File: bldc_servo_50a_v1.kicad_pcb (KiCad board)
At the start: 4 copper layers, 100 x 50 mm, 133 parts, among them J1 CAN1, J2 CAN2, J3 FAN, J4 SWD, J5 SWD, P1 PVDD, P2 GND, P3 PHASE_A, P4 PHASE_B, P5 PHASE_C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

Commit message: Placing DRV, Bulk caps, FETs
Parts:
- removed J4: SWD, Connector_PinHeader_2.54mm:PinHeader_1x05_P2.54mm_Vertical
- moved D2 516.9 mm to (-5.00, 93.4)
- moved H1 516.1 mm to (-9.33, 104.2)
- moved H2 516.1 mm to (-9.33, 109.4)
- moved H3 516.1 mm to (-9.33, 114.6)
- moved C47 474.4 mm to (25.4, -53.5)
- moved J3 474.4 mm to (26.1, -65.4)
- moved U6 474.4 mm to (29.4, -55.4)
- moved C53 436.2 mm to (-17.9, 71.5)
- moved R28 436.2 mm to (-18.3, 74.4)
- moved TH1 436.2 mm to (-18.3, 76.4)
- moved C48 435.1 mm to (-39.9, 66.1)
- moved D1 435.1 mm to (-39.9, 62.4)
- moved D3 435.1 mm to (-51.6, 28.4)
- moved D4 435.1 mm to (-51.6, 32.1)
- moved D5 435.1 mm to (-51.6, 35.8)
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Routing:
- net GND: track 56.4 -> 0.35 mm
- net PVDD: track 0.00 -> 1.00 mm

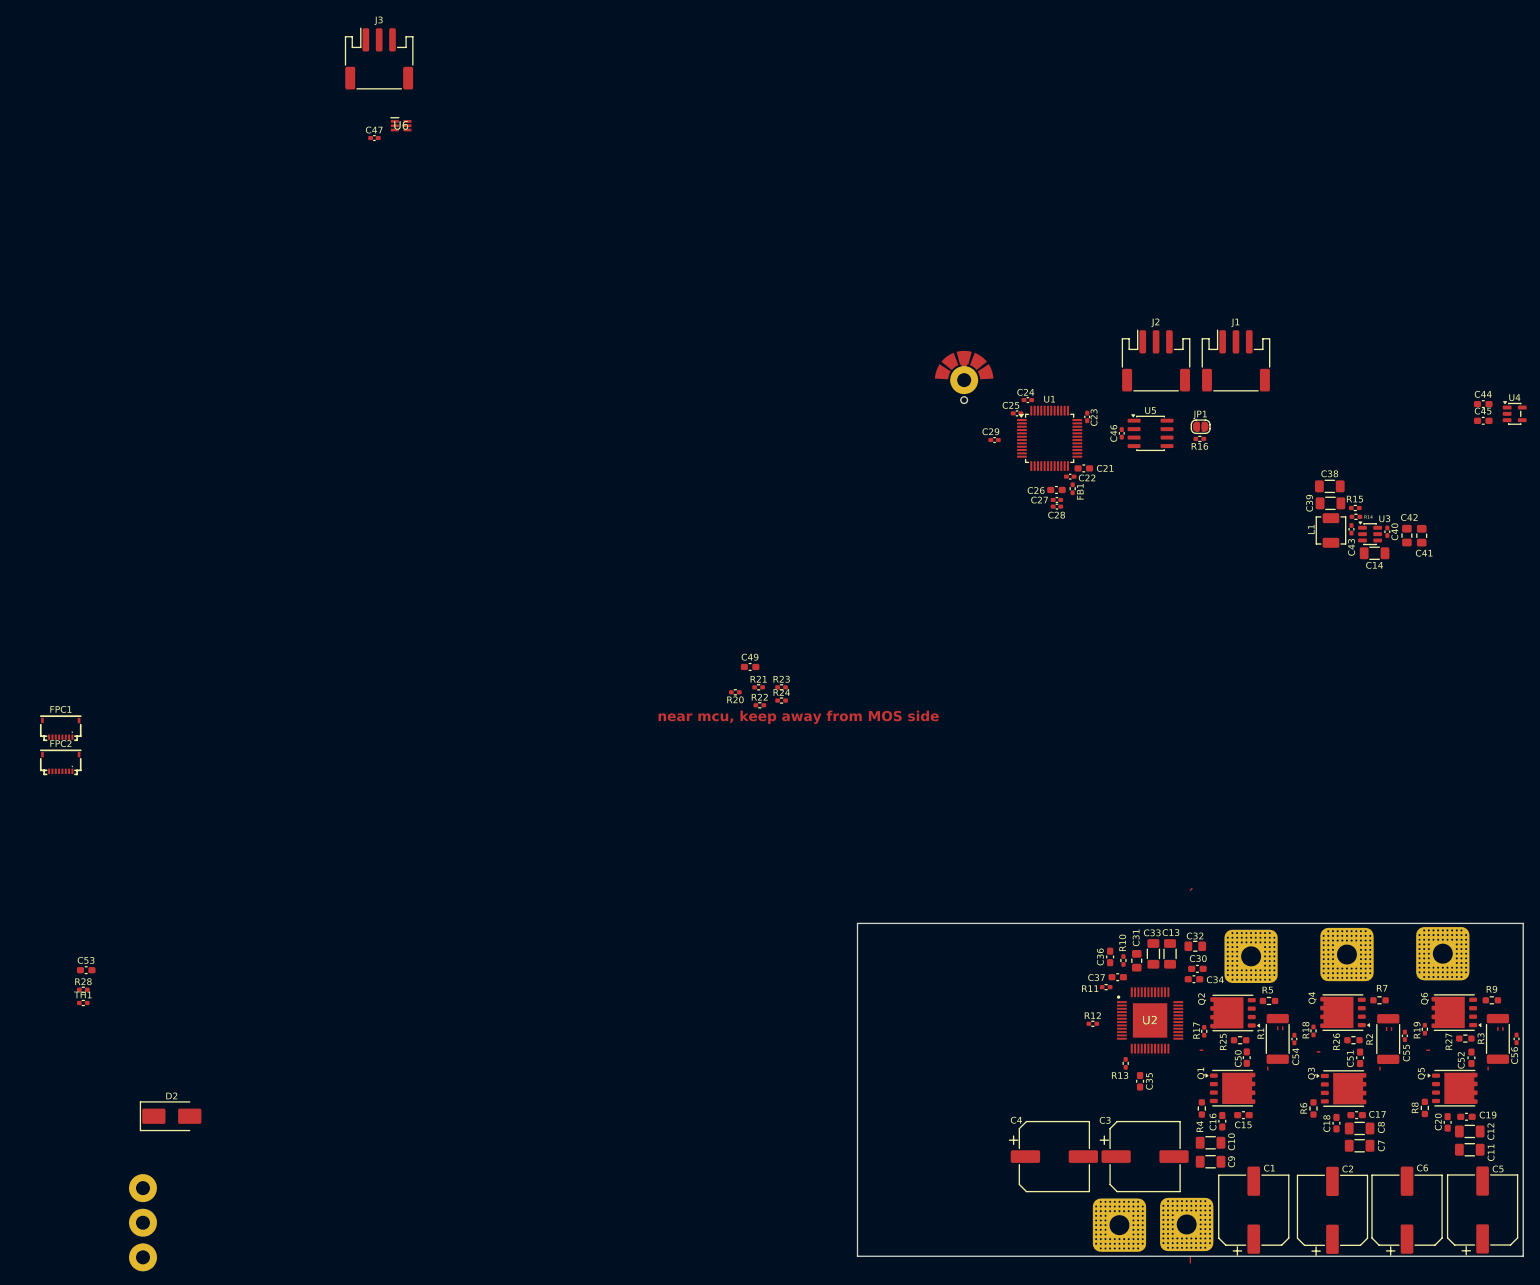
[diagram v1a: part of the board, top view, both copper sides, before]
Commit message: Some more component placement
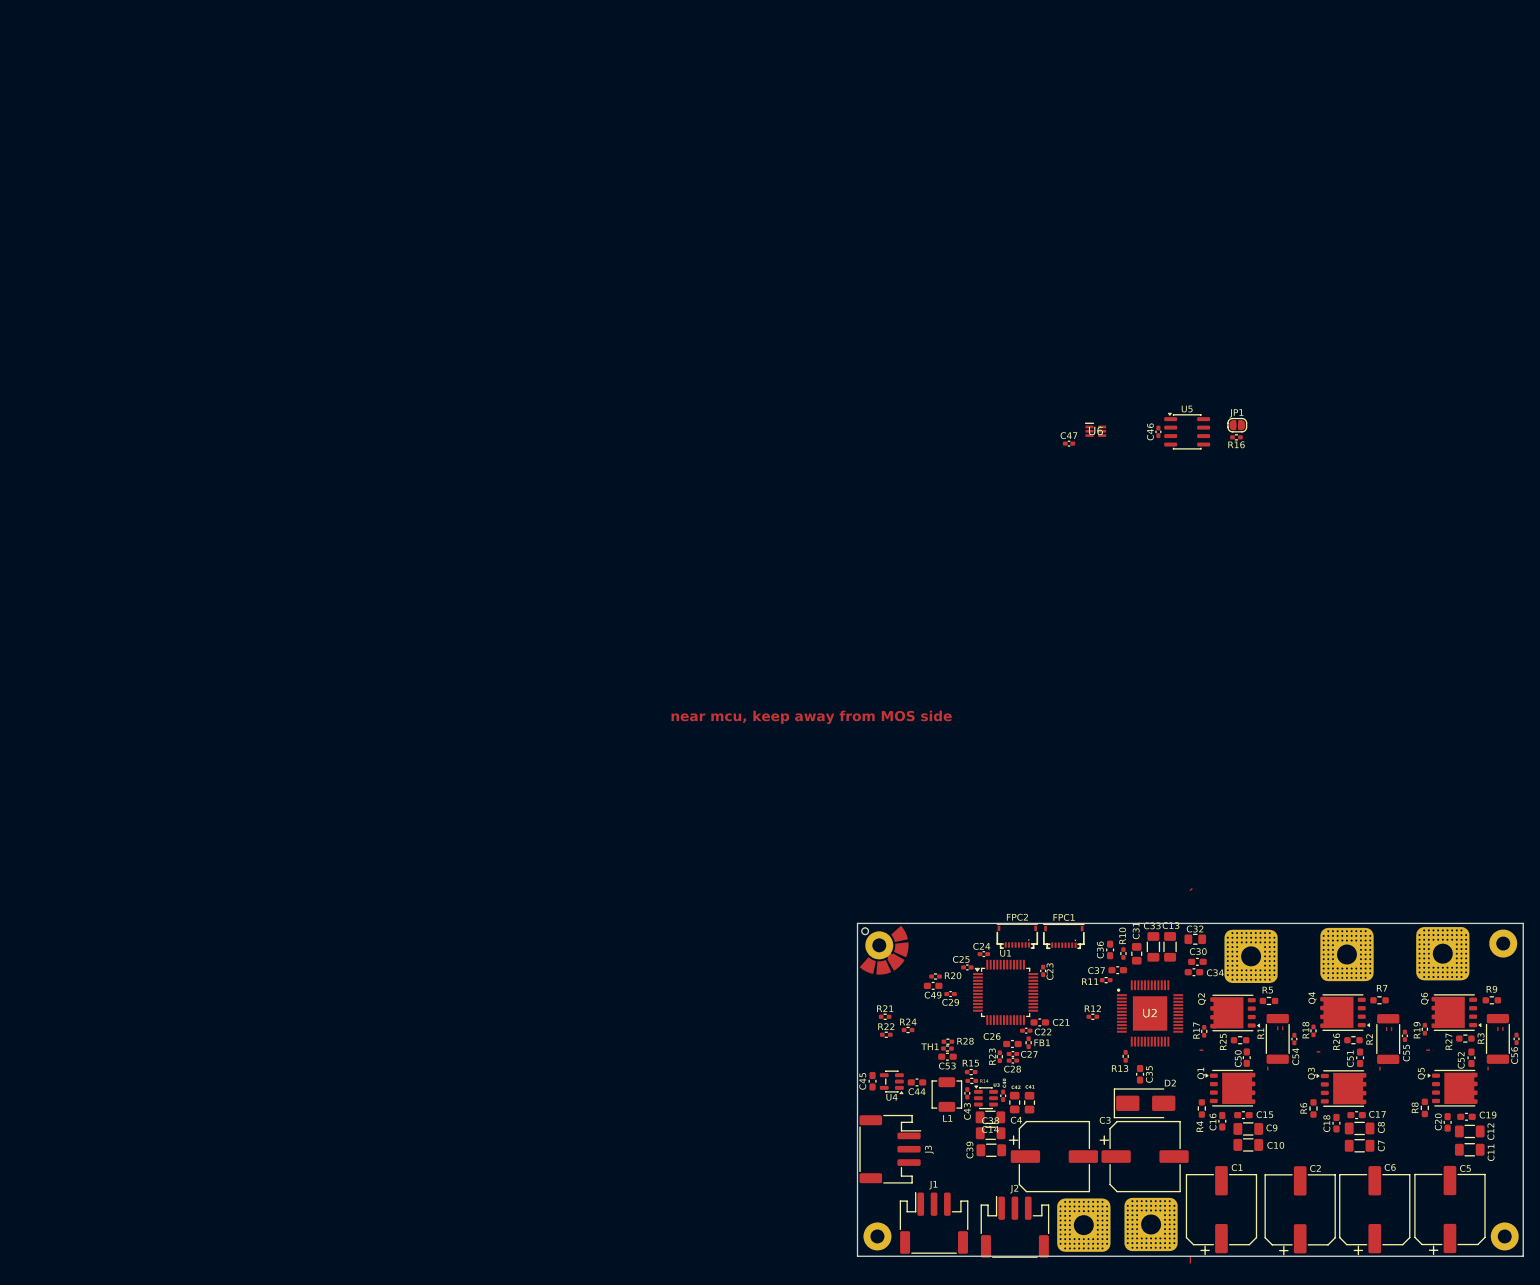
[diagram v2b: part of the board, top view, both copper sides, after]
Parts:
- moved H1 207.6 mm to (195.0, 67.5)
- moved H2 204.6 mm to (195.2, 111.5)
- moved J3 180.9 mm to (102.9, 98.4), turned to -90 degrees
- moved FPC1 153.9 mm to (129.0, 66.5)
- moved D2 146.3 mm to (141.3, 91.5)
- moved FPC2 146.0 mm to (122.0, 66.5)
- moved J1 137.2 mm to (109.5, 109.5)
- moved U4 137.2 mm to (103.2, 88.2), turned to 180 degrees
- moved C45 135.1 mm to (100.3, 88.2), turned to 90 degrees
- moved C44 132.7 mm to (106.9, 88.4), turned to 180 degrees
- moved J2 131.9 mm to (121.7, 110.1)
- moved R28 130.1 mm to (111.6, 82.2)
- moved C53 130.0 mm to (111.5, 84.5), turned to 180 degrees
- moved TH1 130.0 mm to (111.5, 83.3), turned to 180 degrees
- moved U6 114.0 mm to (133.8, -9.45)
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
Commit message: Some routing done
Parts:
- moved H1 125.7 mm to (319.7, 51.2)
- moved P2 125.7 mm to (256.7, 93.5)
- moved C14 125.7 mm to (242.6, 77.3)
- moved C24 125.7 mm to (241.6, 52.8)
- moved C29 125.7 mm to (236.6, 58.8)
- moved C41 125.7 mm to (248.5, 75.1)
- moved C53 125.7 mm to (236.2, 68.2)
- moved FPC2 125.7 mm to (246.7, 50.2)
- moved J5 125.7 mm to (225.9, 51.5)
- moved R22 125.7 mm to (227.0, 64.9)
- moved R23 125.7 mm to (244.0, 68.2)
- moved U4 125.7 mm to (227.8, 72.0)
- moved C21 125.7 mm to (250.0, 63.1)
- moved C22 125.7 mm to (248.0, 64.3)
- moved C23 125.7 mm to (250.6, 55.3)
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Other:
- board size 100 x 50 mm -> 100 x 75 mm

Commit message: Placement of caps
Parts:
- moved C14 176.6 mm to (66.4, 88.5)
- moved C21 176.6 mm to (73.8, 74.2)
- moved C22 176.6 mm to (71.8, 75.5)
- moved C23 176.6 mm to (74.4, 66.5)
- moved C24 176.6 mm to (65.4, 64.0)
- moved C25 176.6 mm to (63.0, 66.0)
- moved C26 176.6 mm to (69.7, 77.5)
- moved C27 176.6 mm to (69.8, 79.0)
- moved C28 176.6 mm to (69.8, 80.0)
- moved C29 176.6 mm to (60.4, 70.0)
- moved C38 176.6 mm to (66.5, 90.9)
- moved C39 176.6 mm to (66.6, 93.4)
- moved C40 176.6 mm to (68.4, 85.3)
- moved C41 176.6 mm to (72.3, 86.3)
- moved C42 176.6 mm to (70.1, 86.3)
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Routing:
- net PVDD: track 1.00 -> 0.00 mm

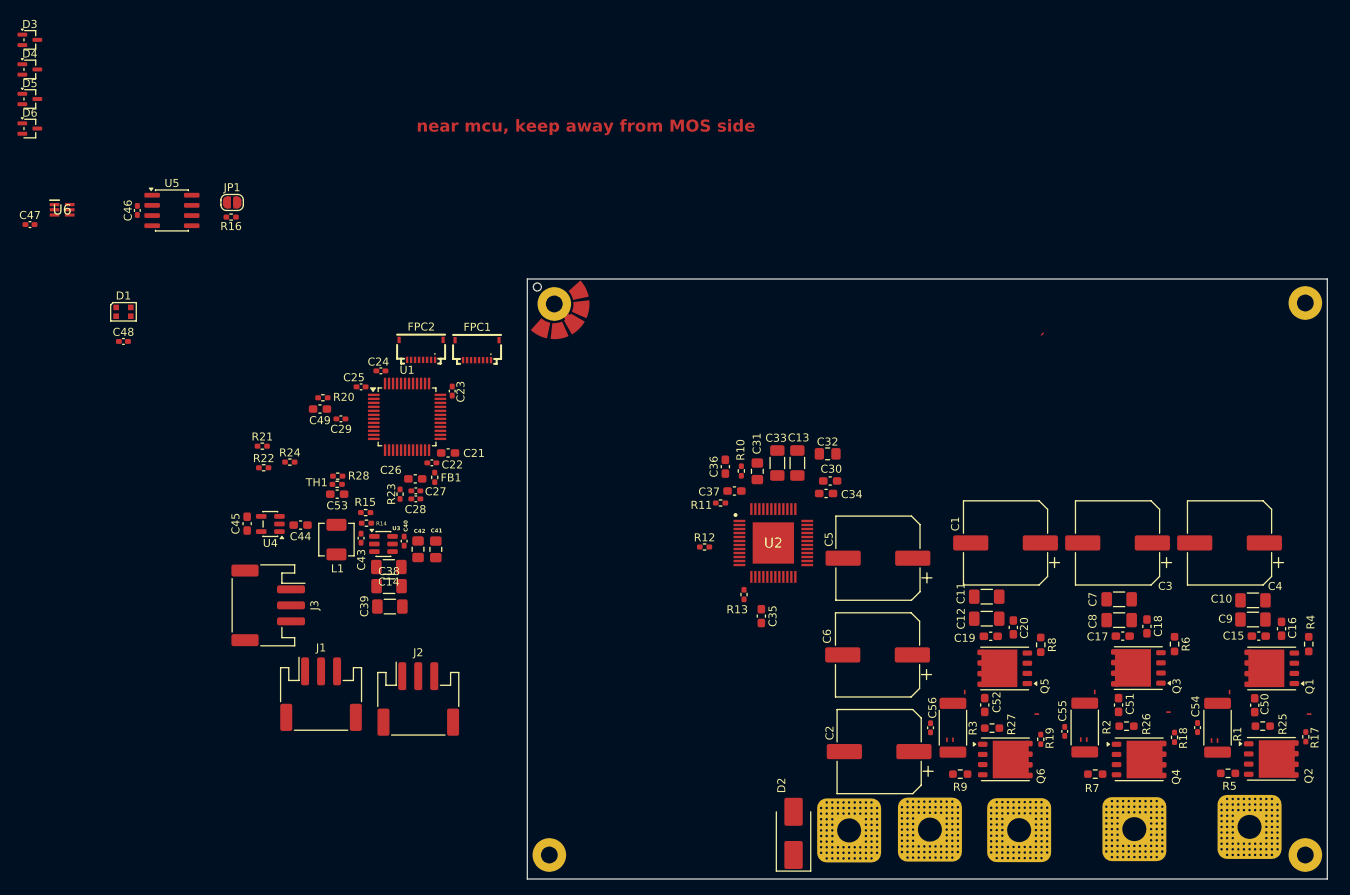
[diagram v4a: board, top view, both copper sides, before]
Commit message: Placement changed
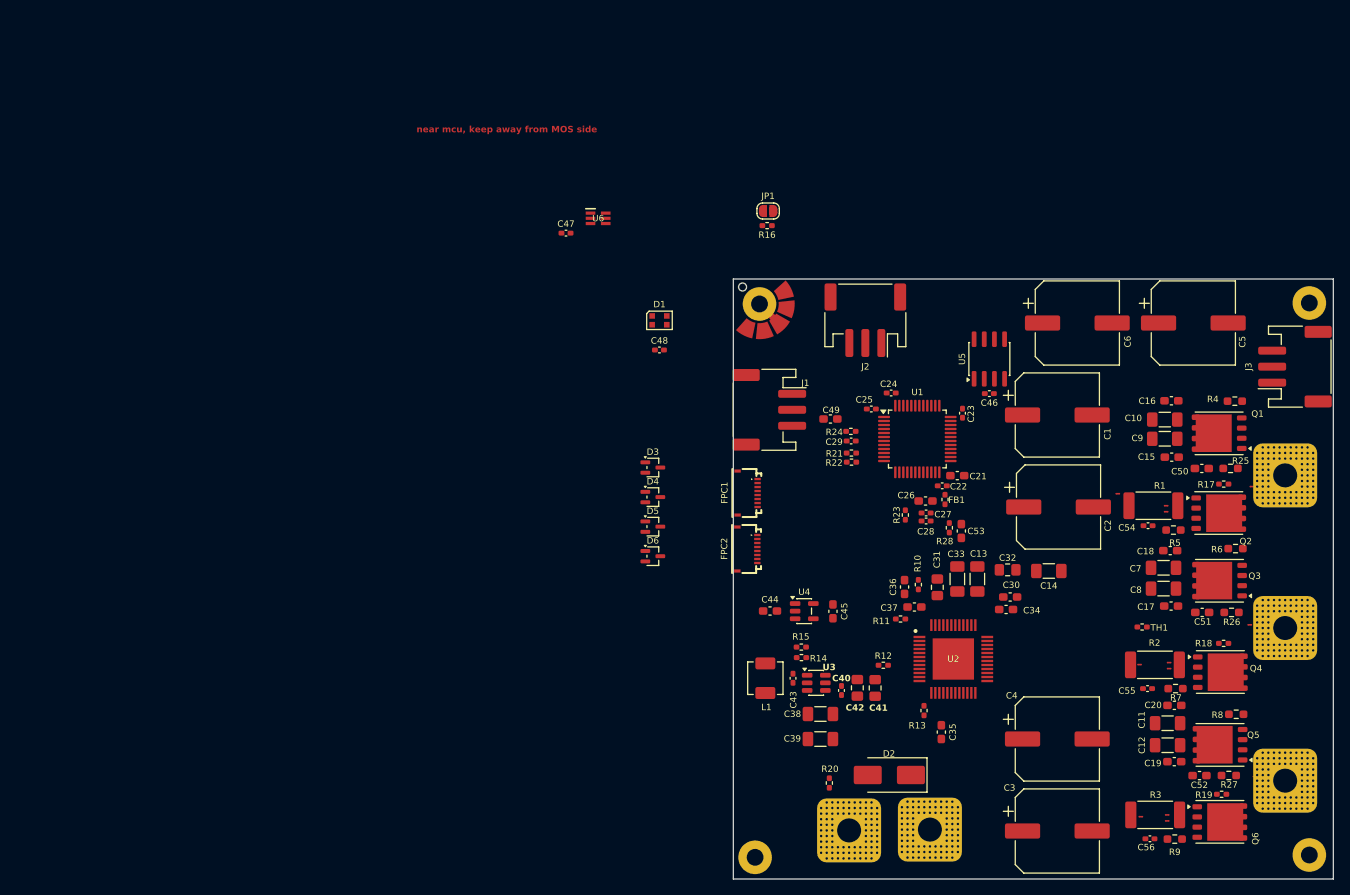
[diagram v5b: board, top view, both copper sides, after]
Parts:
- moved J3 131.8 mm to (179.7, 63.5), turned to 90 degrees
- moved C46 108.9 mm to (141.5, 66.8), turned to 180 degrees
- moved U5 103.8 mm to (141.5, 62.5), turned to 90 degrees
- moved TH1 102.2 mm to (160.6, 96.0), turned to 0 degrees
- moved D3 94.5 mm to (99.4, 76.1)
- moved D4 94.5 mm to (99.4, 79.8)
- moved D5 94.5 mm to (99.4, 83.5)
- moved D6 94.5 mm to (99.4, 87.2)
- moved C14 82.5 mm to (148.9, 89.0)
- moved R20 79.5 mm to (121.5, 115.5), turned to 90 degrees
- moved C53 78.2 mm to (138.0, 84.0), turned to -90 degrees
- moved R28 76.7 mm to (136.5, 83.6), turned to 90 degrees
- moved C45 74.0 mm to (122.0, 94.0), turned to -90 degrees
- moved R21 73.6 mm to (124.3, 74.3), turned to 180 degrees
- moved R22 73.5 mm to (124.3, 75.4), turned to 180 degrees
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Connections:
- net Net-(Q2-S_1) renamed /SP1_TOP
- net Net-(Q4-S_1) renamed /SP2_TOP
- net Net-(Q6-S_1) renamed /SP3_TOP
- J1 pad MP: unconnected-(J1-MountPin-PadMP) -> GND
- J2 pad MP: unconnected-(J2-MountPin-PadMP)_1 -> GND
- J3 pad MP: unconnected-(J3-MountPin-PadMP)_1 -> GND
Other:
- board size 100 x 75 mm -> 75 x 75 mm
